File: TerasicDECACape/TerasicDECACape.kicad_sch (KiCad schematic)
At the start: 33 parts, among them CN1 NASB0-S6701-TS50, CN2 NASB0-S6701-TS50, J1 MiSTer SDRAM Module, J2 USB_A, J3 Conn_01x03_Male, J4 Conn_02x06_Odd_Even, P8 BeagleBone_Black_Header, P9 BeagleBone_Black_Header, SW1 TS-1187A-B-A-B, SW2 TS-1187A-B-A-B

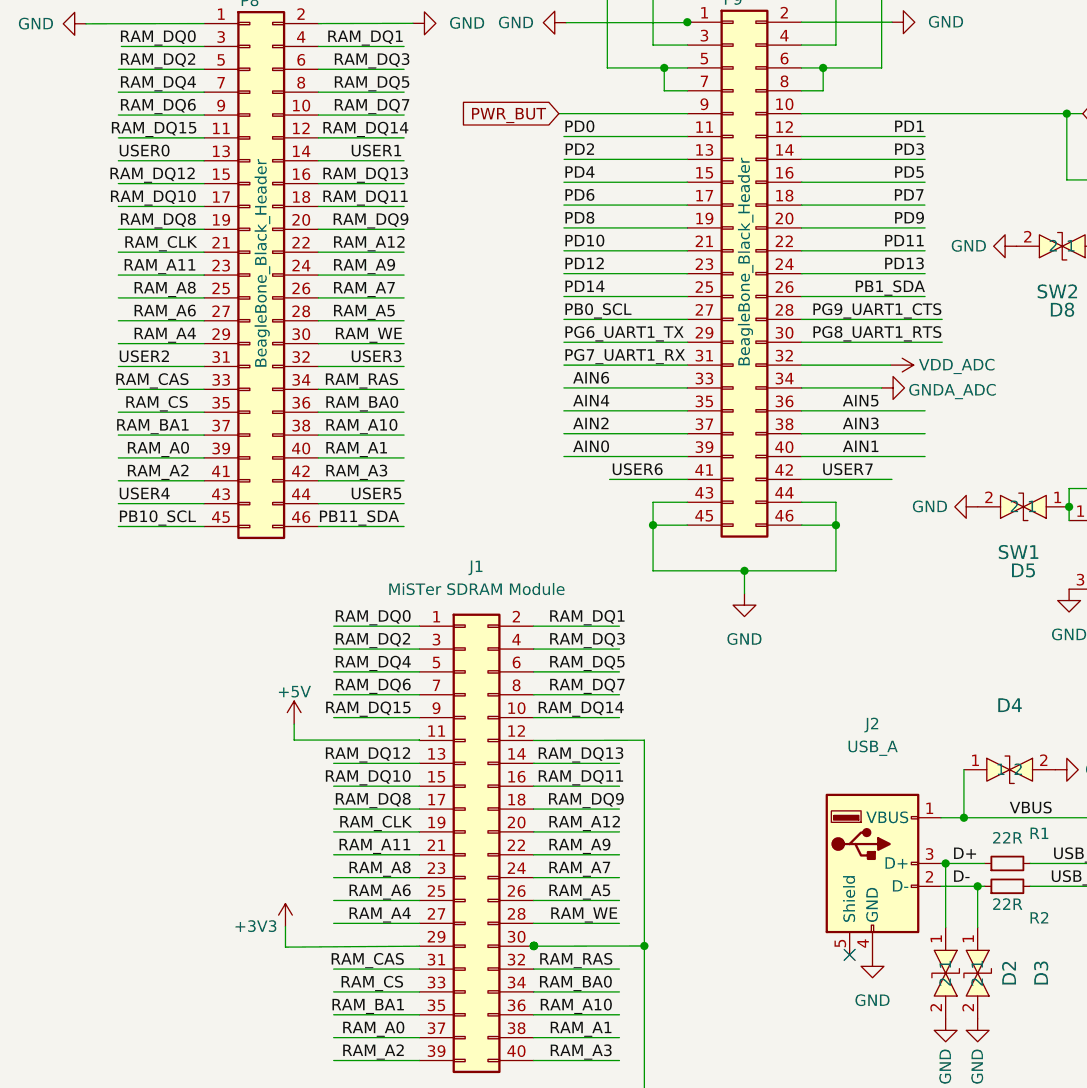
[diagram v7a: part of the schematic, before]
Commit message: fix swapped SDRAM net names on both headers, fix impedance on USB diff pair, add SPI termination resistors
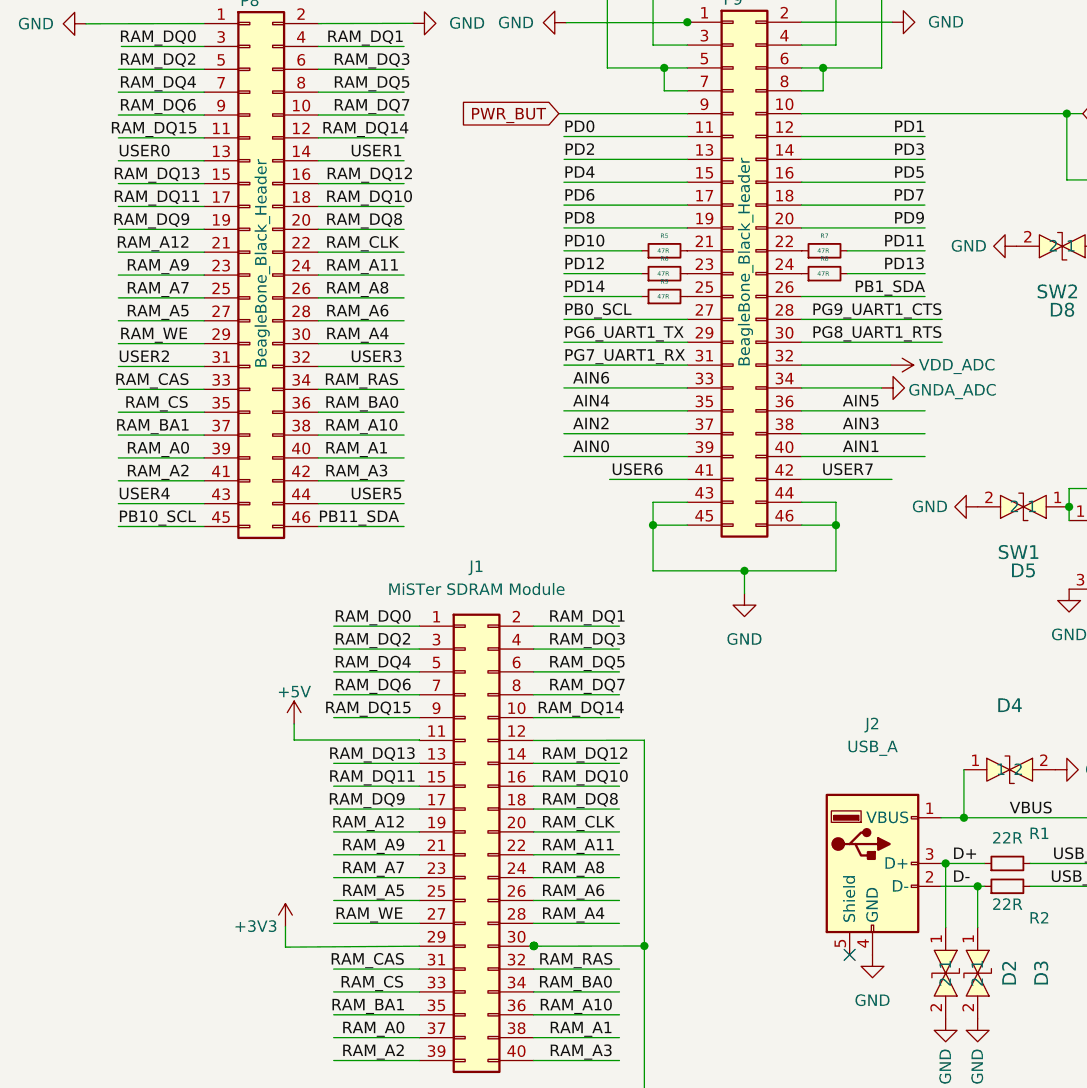
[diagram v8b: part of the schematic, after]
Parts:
- added R5, R6, R7, R8, R9: 47R, R_0402_1005Metric, symbol jlcpcb-basic-resistor-0402:47R
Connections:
- net PD10: now also R5.1; no longer P9.21 (Pin_21)
- net PD11: now also R7.2; no longer P9.22 (Pin_22)
- net PD12: now also R6.1; no longer P9.23 (Pin_23)
- net PD13: now also R8.2; no longer P9.24 (Pin_24)
- net PD14: now also R9.1; no longer P9.25 (Pin_25)
- net RAM_A11: now also J1.22 (Pin_22), P8.24 (Pin_24); no longer J1.21 (Pin_21), P8.23 (Pin_23)
- net RAM_A12: now also J1.19 (Pin_19), P8.21 (Pin_21); no longer J1.20 (Pin_20), P8.22 (Pin_22)
- net RAM_A4: now also J1.28 (Pin_28), P8.30 (Pin_30); no longer J1.27 (Pin_27), P8.29 (Pin_29)
- net RAM_A5: now also J1.25 (Pin_25), P8.27 (Pin_27); no longer J1.26 (Pin_26), P8.28 (Pin_28)
- net RAM_A6: now also J1.26 (Pin_26), P8.28 (Pin_28); no longer J1.25 (Pin_25), P8.27 (Pin_27)
- net RAM_A7: now also J1.23 (Pin_23), P8.25 (Pin_25); no longer J1.24 (Pin_24), P8.26 (Pin_26)
- net RAM_A8: now also J1.24 (Pin_24), P8.26 (Pin_26); no longer J1.23 (Pin_23), P8.25 (Pin_25)
- net RAM_A9: now also J1.21 (Pin_21), P8.23 (Pin_23); no longer J1.22 (Pin_22), P8.24 (Pin_24)
- net RAM_CLK: now also J1.20 (Pin_20), P8.22 (Pin_22); no longer J1.19 (Pin_19), P8.21 (Pin_21)
- net RAM_DQ10: now also J1.16 (Pin_16), P8.18 (Pin_18); no longer J1.15 (Pin_15), P8.17 (Pin_17)
- net RAM_DQ11: now also J1.15 (Pin_15), P8.17 (Pin_17); no longer J1.16 (Pin_16), P8.18 (Pin_18)
- net RAM_DQ12: now also J1.14 (Pin_14), P8.16 (Pin_16); no longer J1.13 (Pin_13), P8.15 (Pin_15)
- net RAM_DQ13: now also J1.13 (Pin_13), P8.15 (Pin_15); no longer J1.14 (Pin_14), P8.16 (Pin_16)
- net RAM_DQ8: now also J1.18 (Pin_18), P8.20 (Pin_20); no longer J1.17 (Pin_17), P8.19 (Pin_19)
- net RAM_DQ9: now also J1.17 (Pin_17), P8.19 (Pin_19); no longer J1.18 (Pin_18), P8.20 (Pin_20)
- net RAM_WE: now also J1.27 (Pin_27), P8.29 (Pin_29); no longer J1.28 (Pin_28), P8.30 (Pin_30)
- new net: P9.21 (Pin_21), R5.2
- new net: P9.22 (Pin_22), R7.1
- new net: P9.23 (Pin_23), R6.2
- new net: P9.24 (Pin_24), R8.1
- new net: P9.25 (Pin_25), R9.2
